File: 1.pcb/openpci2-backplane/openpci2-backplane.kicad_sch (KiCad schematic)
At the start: 10 parts

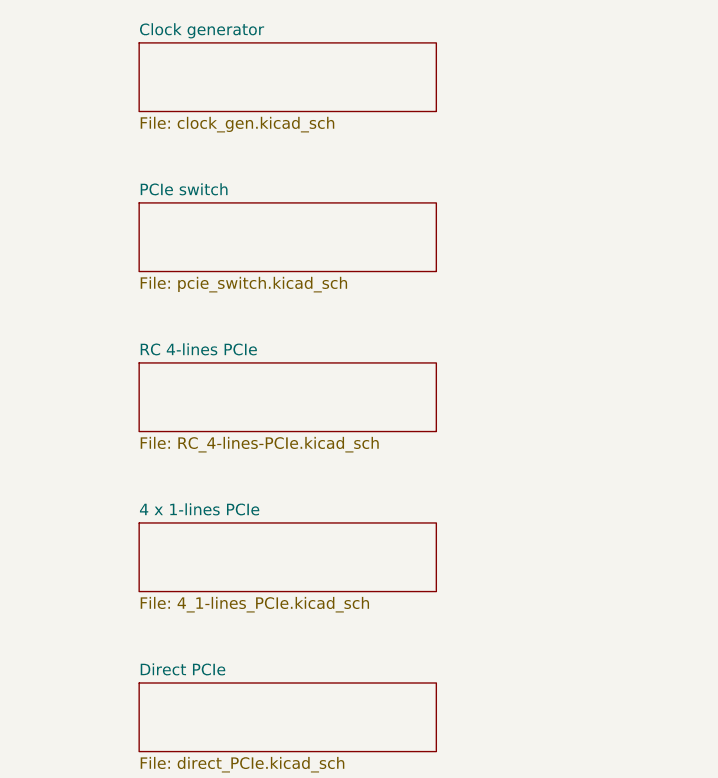
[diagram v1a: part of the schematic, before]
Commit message: PoL converters added
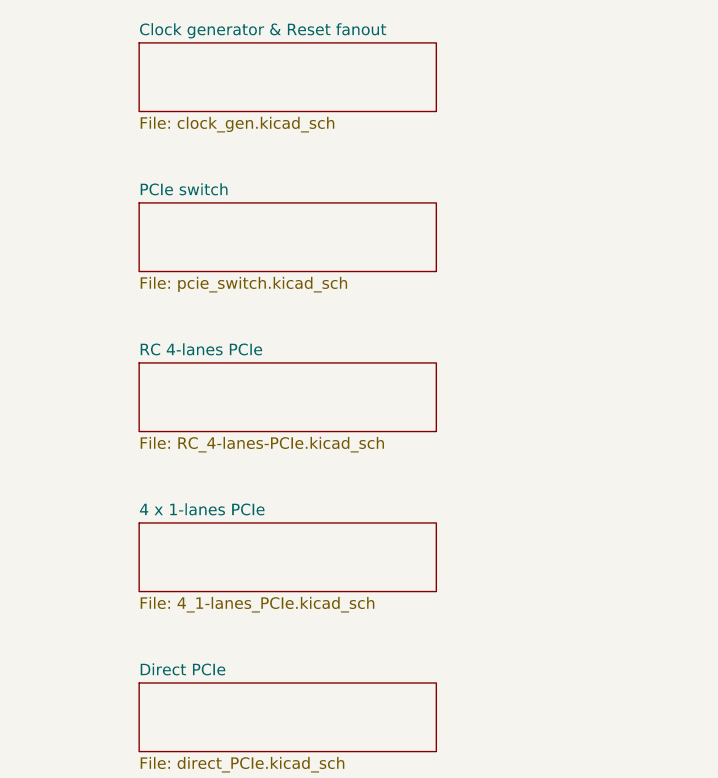
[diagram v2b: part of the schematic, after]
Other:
- sheet 4 x 1-lines PCIe renamed 4 x 1-lanes PCIe
- sheet Clock generator renamed Clock generator & Reset fanout
- sheet RC 4-lines PCIe renamed RC 4-lanes PCIe
- sheet 4 x 1-lanes PCIe: file 4_1-lines_PCIe.kicad_sch -> 4_1-lanes_PCIe.kicad_sch
- sheet RC 4-lanes PCIe: file RC_4-lines-PCIe.kicad_sch -> RC_4-lanes-PCIe.kicad_sch
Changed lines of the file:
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@@
 			(color 0 0 0 0.0000)
 		)
-		(property "Sheetname" "Clock generator"
+		(property "Sheetname" "Clock generator & Reset fanout"
 			(at 30.48 27.2284 0)
 			(effects
@@
 			(color 0 0 0 0.0000)
 		)
-		(property "Sheetname" "RC 4-lines PCIe"
+		(property "Sheetname" "RC 4-lanes PCIe"
 			(at 30.48 62.7884 0)
 			(effects
@@
 			)
 		)
-		(property "Sheetfile" "RC_4-lines-PCIe.kicad_sch"
+		(property "Sheetfile" "RC_4-lanes-PCIe.kicad_sch"
 			(at 30.48 71.7046 0)
 			(effects
@@
 			(color 0 0 0 0.0000)
 		)
-		(property "Sheetname" "4 x 1-lines PCIe"
+		(property "Sheetname" "4 x 1-lanes PCIe"
 			(at 30.48 80.5684 0)
 			(effects
@@
 			)
 		)
-		(property "Sheetfile" "4_1-lines_PCIe.kicad_sch"
+		(property "Sheetfile" "4_1-lanes_PCIe.kicad_sch"
 			(at 30.48 89.4846 0)
 			(effects

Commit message: Few small changes
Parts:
- added LOGO1: Open hardware logo, PCM_EEZ_unsorted:Open HW logo, symbol PCM_EEZ_symbols:Open HW logo
- added LOGO2: NLnet logo, PCM_EEZ_unsorted:NLnet logo, symbol PCM_EEZ_symbols:NLnet logo
- added LOGO3: PCIE2 logo, PCM_Chili-chips:PCIE2 logo, symbol PCM_Chili-chips:PCIE2 logo

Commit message: Various changes
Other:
- sheet 4 x 1-lanes PCIe renamed Switched 4 x 1-lanes PCIe
- sheet Direct PCIe renamed Direct 4-lane PCIe
- sheet RC 4-lanes PCIe renamed RC 1-lane and 2-lane PCIE
- moved on the sheet: H1, H2, H3, H4, H5, H6
